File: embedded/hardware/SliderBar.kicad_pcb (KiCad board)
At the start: 2 copper layers, 35 parts, among them J1 USB_B_Mini, J2 MOTOR_OUT, J3 POT_IN, J4 DEBUG, U1 MIC5205-3.3YM5, U2 TB6612FNG, U3 MT3608, U4 STM32F072C8Tx

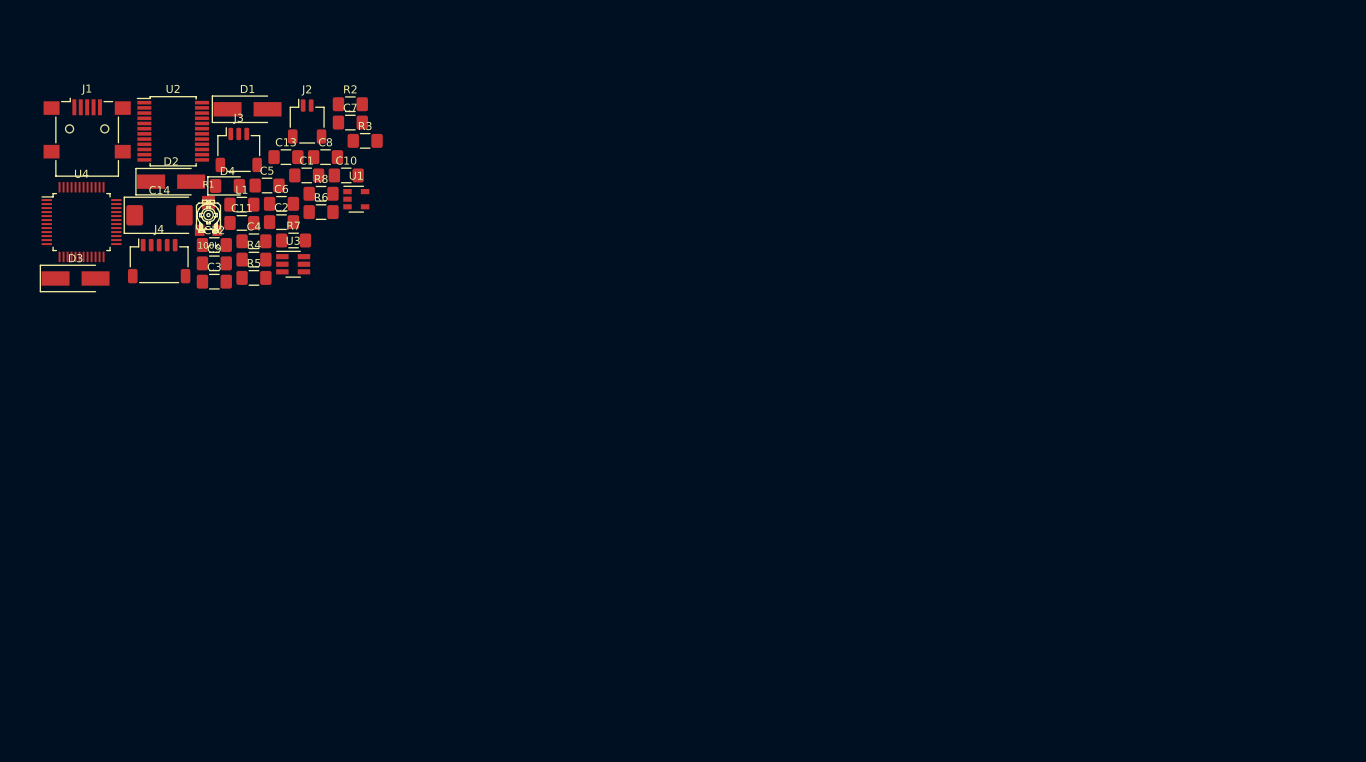
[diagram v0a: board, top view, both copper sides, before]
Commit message: Define board size, place USB connector
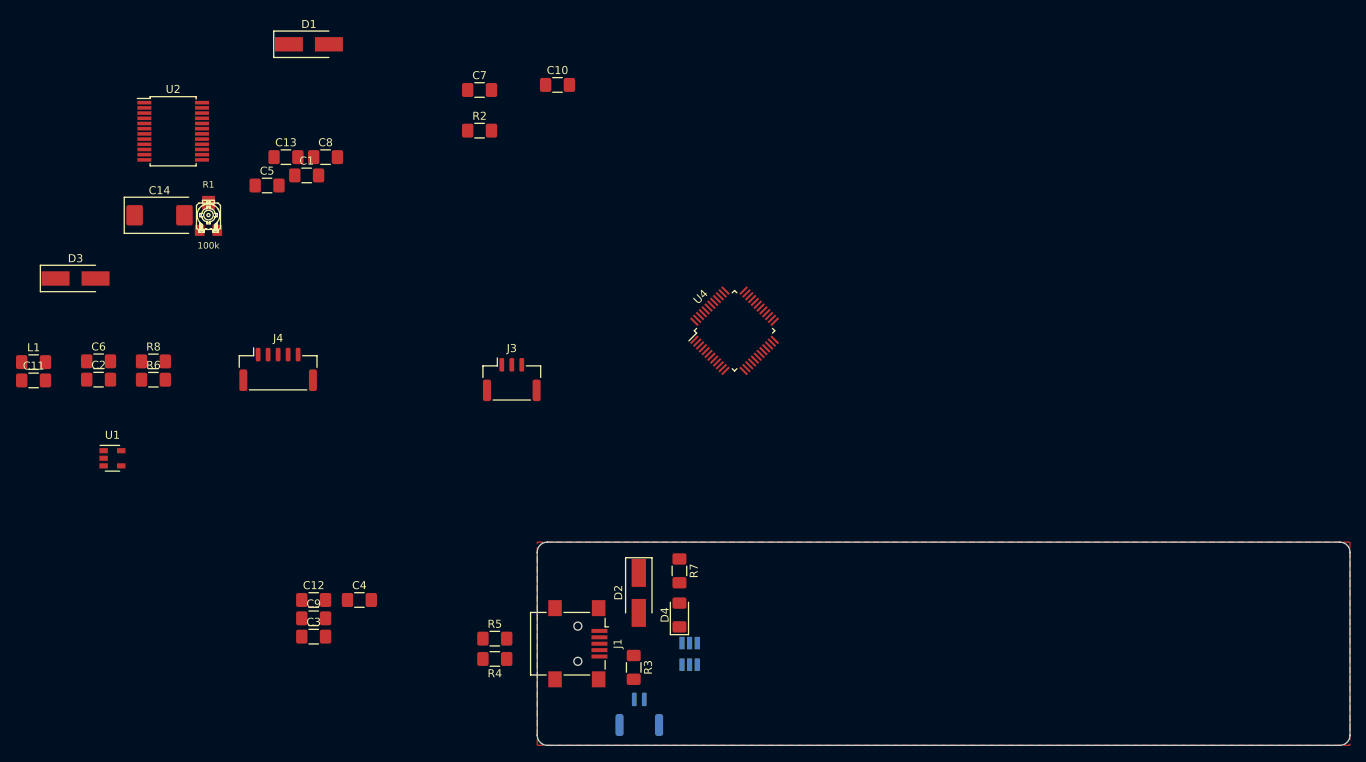
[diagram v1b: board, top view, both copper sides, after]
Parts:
- J2: footprint Connector_JST:JST_SH_SM02B-SRSS-TB_1x02-1MP_P1.00mm_Horizontal -> Connector_JST:JST_GH_SM02B-GHS-TB_1x02-1MP_P1.25mm_Horizontal; moved to B.Cu
- J3: footprint Connector_JST:JST_SH_SM03B-SRSS-TB_1x03-1MP_P1.00mm_Horizontal -> Connector_JST:JST_GH_SM03B-GHS-TB_1x03-1MP_P1.25mm_Horizontal
- J4: footprint Connector_JST:JST_SH_SM05B-SRSS-TB_1x05-1MP_P1.00mm_Horizontal -> Connector_JST:JST_GH_SM05B-GHS-TB_1x05-1MP_P1.25mm_Horizontal
- U3: moved to B.Cu
- moved J1 88.9 mm to (100.3, 96.5), turned to 270 degrees
- moved J2 84.9 mm to (108.0, 105.3), turned to 180 degrees
- moved U4 82.7 mm to (119.9, 57.4), turned to 45 degrees
- moved D4 77.9 mm to (113.0, 92.9), turned to 90 degrees
- moved D2 77.8 mm to (108.0, 90.2), turned to 270 degrees
- moved R3 73.9 mm to (107.3, 99.5), turned to 270 degrees
- moved U3 69.5 mm to (114.3, 97.8), turned to 90 degrees
- moved R7 63.5 mm to (113.0, 87.4), turned to 270 degrees
- moved R4 58.3 mm to (90.0, 98.4), turned to 180 degrees
- moved R5 54.2 mm to (90.0, 95.9)
- moved C4 46.7 mm to (73.0, 91.1)
- moved C12 46.1 mm to (67.3, 91.1)
- moved C3 46.1 mm to (67.3, 95.6)
- moved C9 46.1 mm to (67.3, 93.3)
- moved J3 44.6 mm to (92.1, 63.5)
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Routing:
- added copper zone on F.Cu, net GND
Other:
- board outline added: 101.6 x 25.4 mm
- net class Default: clearance 0.2 -> 0.13; via_dia 0.8 -> 0.6; via_drill 0.4 -> 0.3
- net class Power added: clearance 0.13, trace_width 1, via_dia 1.6, via_drill 0.8
- rule pad_to_mask_clearance: 0 -> 0.0502
- rule trace_clearance: 0.2 -> 0.13
- rule trace_min: 0.2 -> 0.0889
- rule via_min_drill: 0.3 -> 0.2
- rule via_min_size: 0.4 -> 0.6
